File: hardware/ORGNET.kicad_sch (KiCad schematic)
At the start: 43 parts, among them J1 Conn_02x08_Odd_Even, J3 Conn_01x03, U1 SN74LVC8T245, U2 SN74LVC8T245, U3 AP2112K-3.3, U4 RP2350A, U5 W25Q128JVP, U6 Raspberry Pi Radio Module 2, Y1 12M

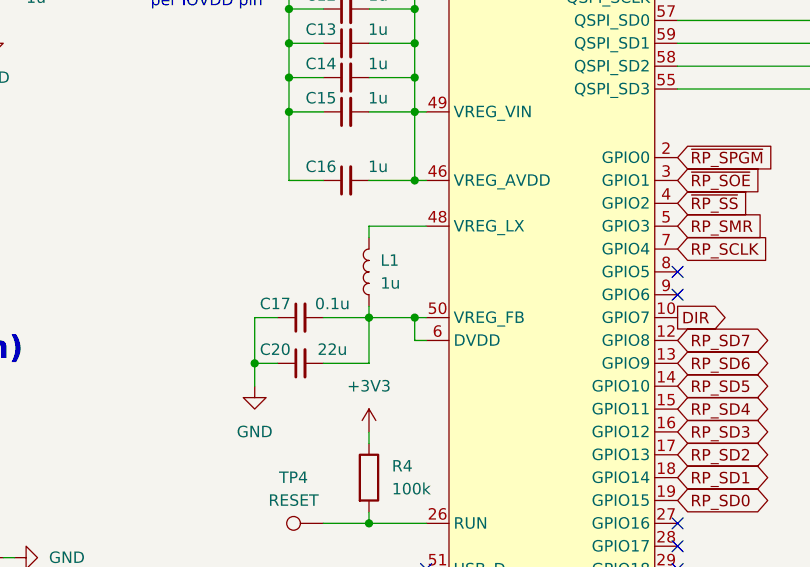
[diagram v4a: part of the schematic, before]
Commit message: Fix power routing to address short circuiting issue
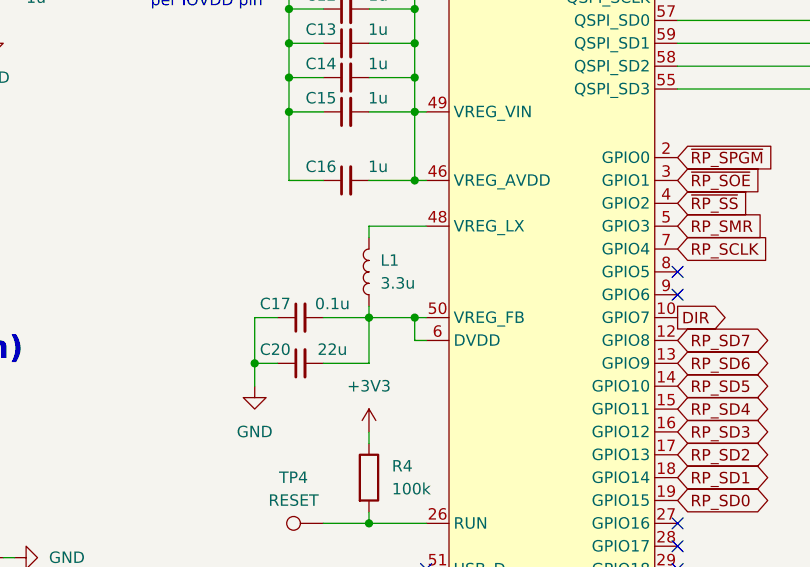
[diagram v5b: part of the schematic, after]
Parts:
- L1: value 1u -> 3.3u; footprint Inductor_SMD:L_1008_2520Metric_Pad1.43x2.20mm_HandSolder -> Inductor_SMD:L_1210_3225Metric_Pad1.42x2.65mm_HandSolder
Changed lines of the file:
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@@
 			)
 		)
-		(property "Value" "1u"
+		(property "Value" "3.3u"
 			(at 153.67 74.9299 0)
 			(effects
@@
 			)
 		)
-		(property "Footprint" "Inductor_SMD:L_1008_2520Metric_Pad1.43x2.20mm_HandSolder"
+		(property "Footprint" "Inductor_SMD:L_1210_3225Metric_Pad1.42x2.65mm_HandSolder"
 			(at 152.4 73.66 0)
 			(effects
